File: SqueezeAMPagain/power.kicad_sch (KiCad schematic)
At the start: 63 parts, among them J6 Conn_01x02_Pin, J7 Barrel_Jack_Switch_MountingPin, Q1 Q_NPN_BEC, Q10 AO3401A, Q3 AO3401A, Q6 Q_NPN_BEC, Q7 AO3401A, Q8 AO3401A, Q9 AO3401A, U5 TPS5430DDA, U7 AMS1117-3.3

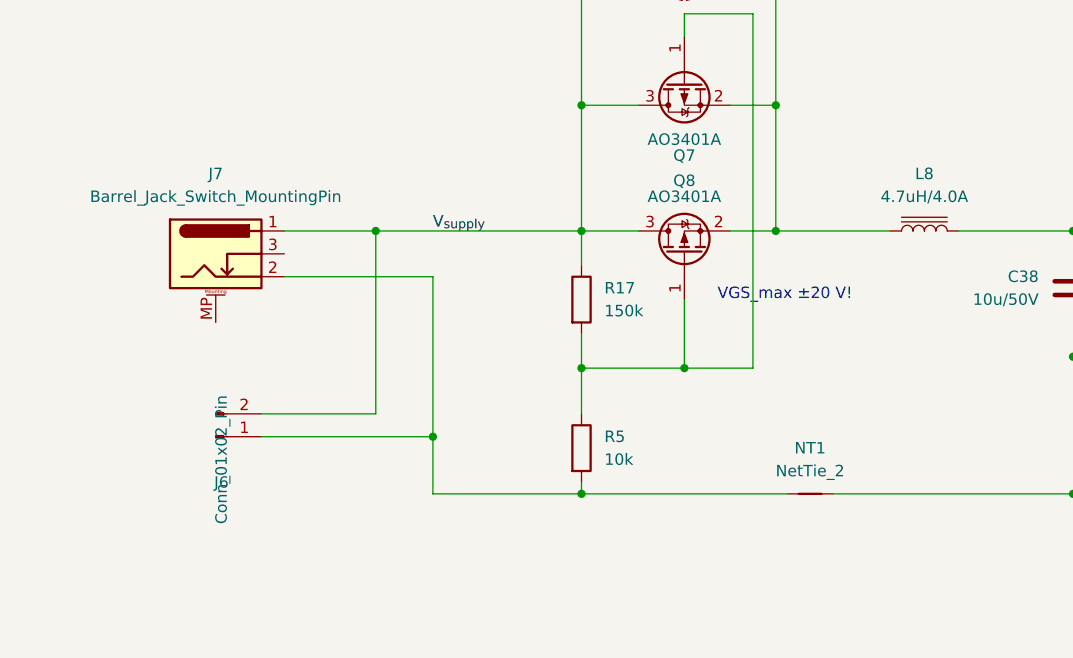
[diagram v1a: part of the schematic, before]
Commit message: Update SqueezeAMPagain.kicad_pcb, SqueezeAMPagain.kicad_prl, SqueezeAMPagain.kicad_pro, and 5 more files
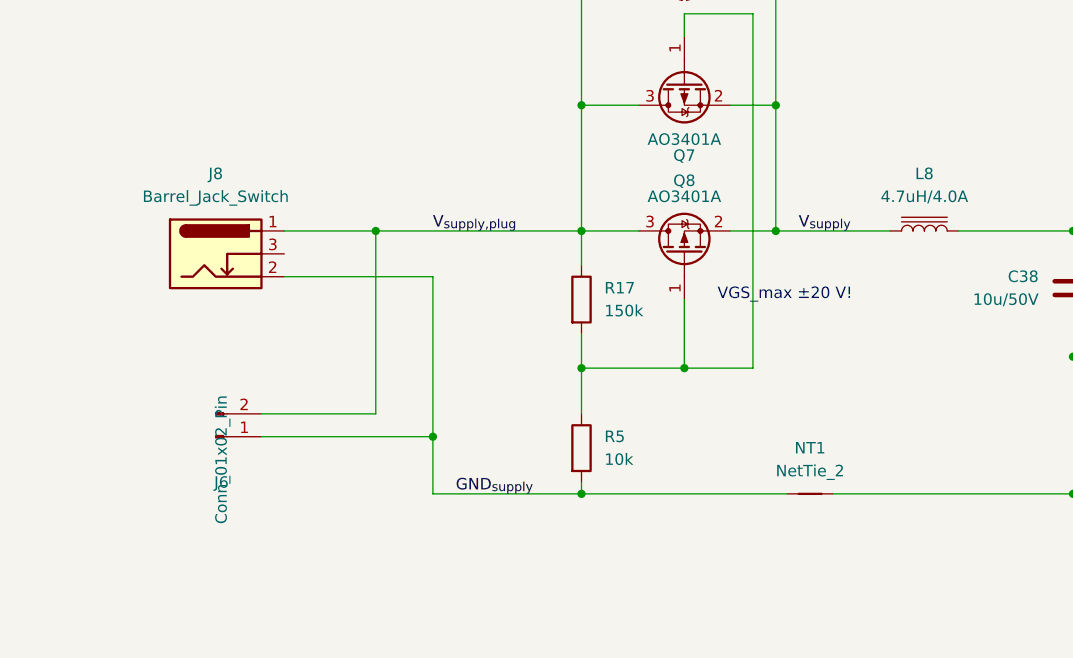
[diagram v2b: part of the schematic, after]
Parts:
- removed J7: Barrel_Jack_Switch_MountingPin, Connector_BarrelJack:BarrelJack_CUI_PJ-079BH_Horizontal, symbol Connector:Barrel_Jack_Switch_MountingPin
- added J8: Barrel_Jack_Switch, Connector_BarrelJack:BarrelJack_CUI_PJ-102AH_Horizontal, symbol Connector:Barrel_Jack_Switch
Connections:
- net V_{supply}: now also JP3.2 (B), L8.1, Q7.2 (S), Q8.2 (S); no longer J6.2 (Pin_2), JP3.1 (A), Q7.3 (D), Q8.3 (D), R17.1
- net GND_{supply}: now reaches J6.1 (Pin_1), NT1.1, R5.2
- net GND_{supply}: now also J8.2
- new net V_{supply,plug}: J6.2 (Pin_2), J8.1, JP3.1 (A), Q7.3 (D), Q8.3 (D), R17.1
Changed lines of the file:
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@@
 		)
 	)
+	(label "GND_{supply}"
+		(at 60.96 82.55 0)
+		(fields_autoplaced yes)
+		(effects
+			(font
+				(size 1.27 1.27)
+			)
+			(justify left bottom)
+		)
+	)
 	(label "PH"
 		(at 168.91 123.19 0)
@@
 	)
 	(label "V_{supply}"
+		(at 99.06 53.34 0)
+		(fields_autoplaced yes)
+		(effects
+			(font
+				(size 1.27 1.27)
+			)
+			(justify left bottom)
+		)
+	)
+	(label "V_{supply,plug}"
 		(at 58.42 53.34 0)
 		(fields_autoplaced yes)
@@
 		(length 2.54)
 		(shape round)
+		(at 82.55 177.8 0)
+		(fields_autoplaced yes)
+		(effects
+			(font
+				(size 1.27 1.27)
+			)
+			(justify left bottom)
+		)
+		(property "Netclass" "Supply"
+			(at 83.2485 175.26 0)
+			(effects
+				(font
+					(size 1.27 1.27)
+					(italic yes)
+				)
+				(justify left)
+			)
+		)
+	)
+	(netclass_flag ""
+		(length 2.54)
+		(shape round)
 		(at 153.67 53.34 0)
 		(fields_autoplaced yes)
@@
 	)
 	(symbol
-		(lib_id "Connector:Barrel_Jack_Switch_MountingPin")
-		(at 34.29 55.88 0)
-		(unit 1)
-		(exclude_from_sim no)
-		(in_bom yes)
-		(on_board yes)
-		(dnp no)
-		(fields_autoplaced yes)
-		(property "Reference" "J7"
-			(at 34.29 46.99 0)
-			(effects
-				(font
-					(size 1.27 1.27)
-				)
-			)
-		)
-		(property "Value" "Barrel_Jack_Switch_MountingPin"
-			(at 34.29 49.53 0)
-			(effects
-				(font
-					(size 1.27 1.27)
-				)
-			)
-		)
-		(property "Footprint" "Connector_BarrelJack:BarrelJack_CUI_PJ-079BH_Horizontal"
-			(at 35.56 56.896 0)
-			(effects
-				(font
-					(size 1.27 1.27)
-				)
-				(hide yes)
-			)
-		)
-		(property "Datasheet" "~"
-			(at 35.56 56.896 0)
-			(effects
-				(font
-					(size 1.27 1.27)
-				)
-				(hide yes)
-			)
-		)
-		(property "Description" "DC Barrel Jack with an internal switch and a mounting pin"
-			(at 34.29 55.88 0)
-			(effects
-				(font
-					(size 1.27 1.27)
-				)
-				(hide yes)
-			)
-		)
-		(pin "1"
-		)
-		(pin "MP"
-		)
-		(pin "3"
-		)
-		(pin "2"
-		)
-		(instances
-			(project ""
-				(path "/3675160b-d9e5-490e-b506-2a7966e79ed0/0f57a469-41de-4f06-810e-cfdb6f5b9e50"
-					(reference "J7")
-					(unit 1)
-				)
-			)
-		)
-	)
-	(symbol
 		(lib_id "power:GND")
 		(at 147.32 153.67 0)
@@
 					(unit 1)
 				)
+			)
+		)
+	)
+	(symbol
+		(lib_id "Connector:Barrel_Jack_Switch")
+		(at 34.29 55.88 0)
+		(unit 1)
+		(exclude_from_sim no)
+		(in_bom yes)
+		(on_board yes)
+		(dnp no)
+		(fields_autoplaced yes)
+		(property "Reference" "J8"
+			(at 34.29 46.99 0)
+			(effects
+				(font
+					(size 1.27 1.27)
+				)
+			)
+		)
+		(property "Value" "Barrel_Jack_Switch"
+			(at 34.29 49.53 0)
+			(effects
+				(font
+					(size 1.27 1.27)
+				)
+			)
+		)
+		(property "Footprint" "Connector_BarrelJack:BarrelJack_CUI_PJ-102AH_Horizontal"
+			(at 35.56 56.896 0)
+			(effects
+				(font
+					(size 1.27 1.27)
+				)
+				(hide yes)
+			)
+		)
+		(property "Datasheet" "~"
+			(at 35.56 56.896 0)
+			(effects
+				(font
+					(size 1.27 1.27)
+				)
+				(hide yes)
+			)
+		)
+		(property "Description" "DC Barrel Jack with an internal switch"
+			(at 34.29 55.88 0)
+			(effects
+				(font
+					(size 1.27 1.27)
+				)
+				(hide yes)
+			)
+		)
+		(property "reichelt#" "CLIFF FCR681465P"
+			(at 34.29 55.88 0)
+			(effects
+				(font
+					(size 1.27 1.27)
+				)
+				(hide yes)
+			)
+		)
+		(pin "1"
+		)
+		(pin "3"
+		)
+		(pin "2"
+		)
+		(instances
+			(project ""
+				(path "/3675160b-d9e5-490e-b506-2a7966e79ed0/0f57a469-41de-4f06-810e-cfdb6f5b9e50"
+					(reference "J8")
+					(unit 1)
+				)

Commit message: Update SqueezeAMPagain.kicad_pcb, SqueezeAMPagain.kicad_prl, SqueezeAMPagain.kicad_pro, and 11 more files
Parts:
- renumbered C76 to C59, C81 to C60, C2 to C62, C45 to C63, C71 to C64, C58 to C65, C38 to C66, C6 to C67, C42 to C68, C49 to C69, C51 to C70, C50 to C71, C59 to C72, C4 to C73, C44 to C74, C60 to C75, C43 to C76, C54 to C77, C82 to C78, C8 to C79, C57 to C80, C56 to C81, C83 to C82, D3 to D1, FB7 to FB2, FB2 to FB3, FB5 to FB4, FB1 to FB5, J8 to J6, J6 to J7, JP5 to JP10, JP3 to JP11, JP4 to JP12, JP12 to JP13, L8 to L5, L11 to L6, L9 to L7, Q6 to Q1, Q10 to Q2, Q7 to Q3, Q8 to Q4, Q1 to Q5, Q3 to Q6, Q9 to Q7, R19 to R22, R15 to R23, R18 to R24, R16 to R25, R17 to R26, R5 to R27, R20 to R28, R2 to R29, R4 to R30, R3 to R31, R14 to R32, R12 to R33, R13 to R34, U7 to U5, U5 to U6

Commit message: Update SqueezeAMPagain.kicad_pcb, SqueezeAMPagain.kicad_prl, SqueezeAMPagain.kicad_pro, and 4 more files
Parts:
- added C90: 2.2u/25V, Capacitor_SMD:C_0805_2012Metric, symbol Device:C
- added C91: 100n, Capacitor_SMD:C_0603_1608Metric, symbol Device:C
- added Q10: AO3401A, Package_TO_SOT_SMD:SOT-23, symbol Transistor_FET:AO3401A
- added Q11: Q_NPN_BEC, Package_TO_SOT_SMD:SOT-23, symbol Device:Q_NPN_BEC
- added R40: 150k, Resistor_SMD:R_0603_1608Metric, symbol Device:R
- added R41, R42: 10k, Resistor_SMD:R_0603_1608Metric, symbol Device:R
- D2: value SS34 550mV 2A -> SS34 550mV 2A
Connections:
- net +3.3V: now also Q10.2 (S), R40.1
- net GND: now also C90.2, C91.2, Q11.2 (E), R42.2
- net PON: now also R41.1
- new net: Q10.1 (G), Q11.3 (C), R40.2
- new net: Q11.1 (B), R41.2, R42.1
- new net +3.3V_{SW}: C90.1, C91.1, Q10.3 (D)
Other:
- moved on the sheet: C59, C60, C64, FB3, U5

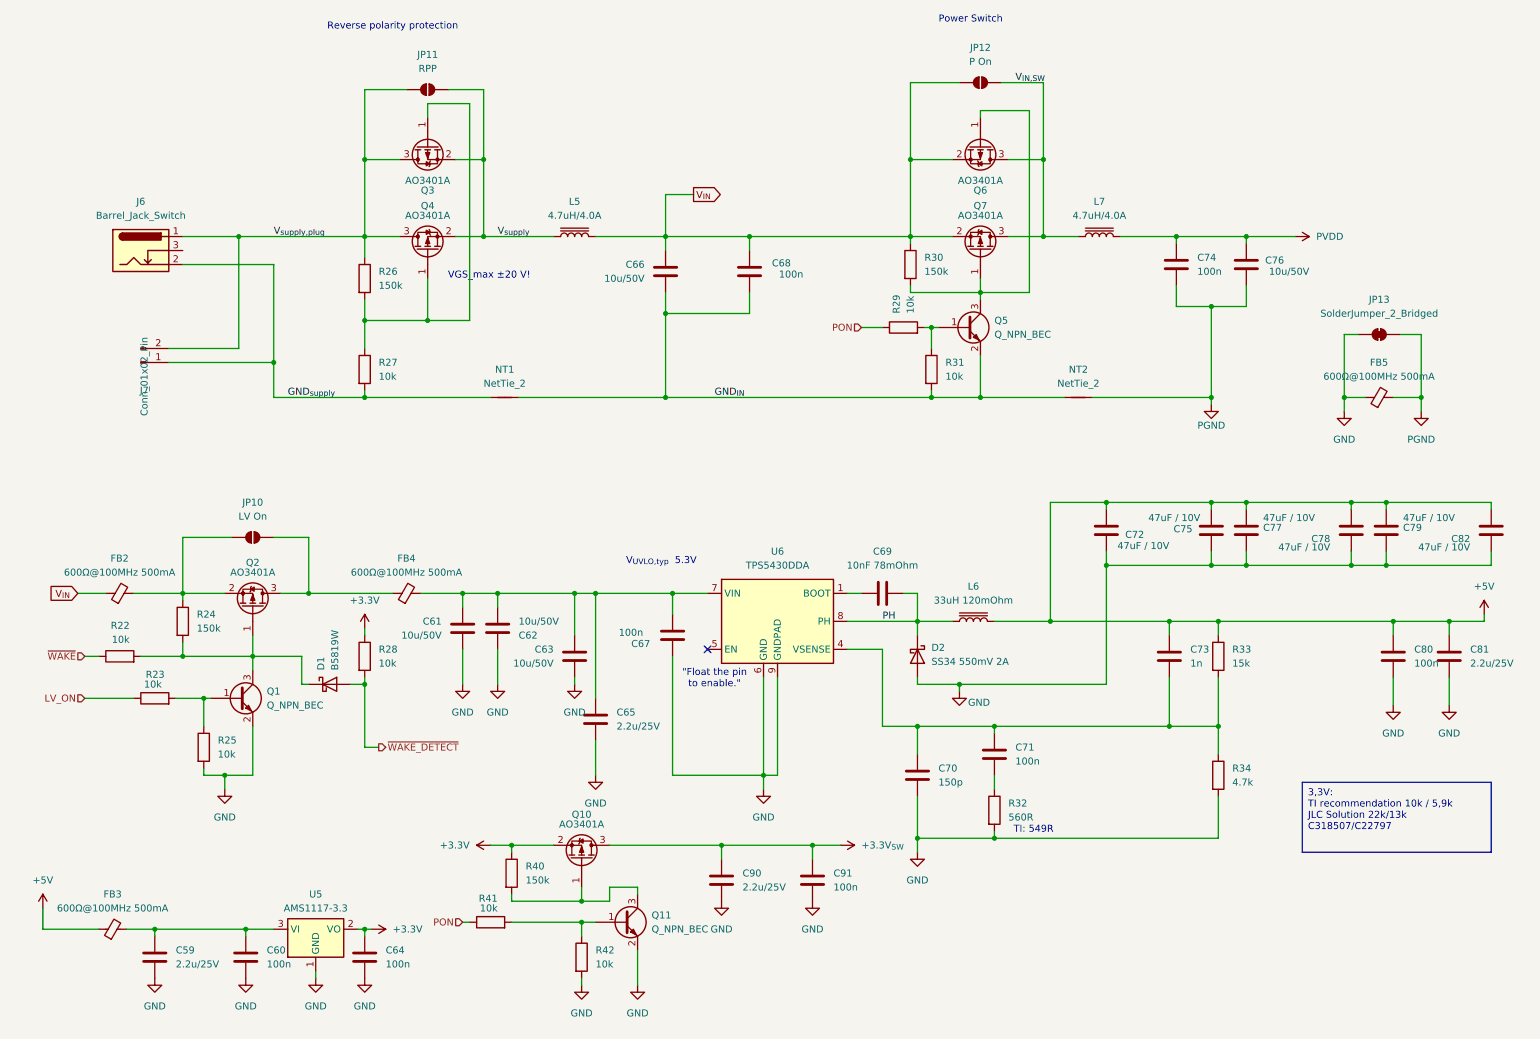
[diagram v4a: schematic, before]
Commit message: Update SqueezeAMPagain.kicad_pcb, SqueezeAMPagain.kicad_prl, SqueezeAMPagain.kicad_pro, and 5 more files
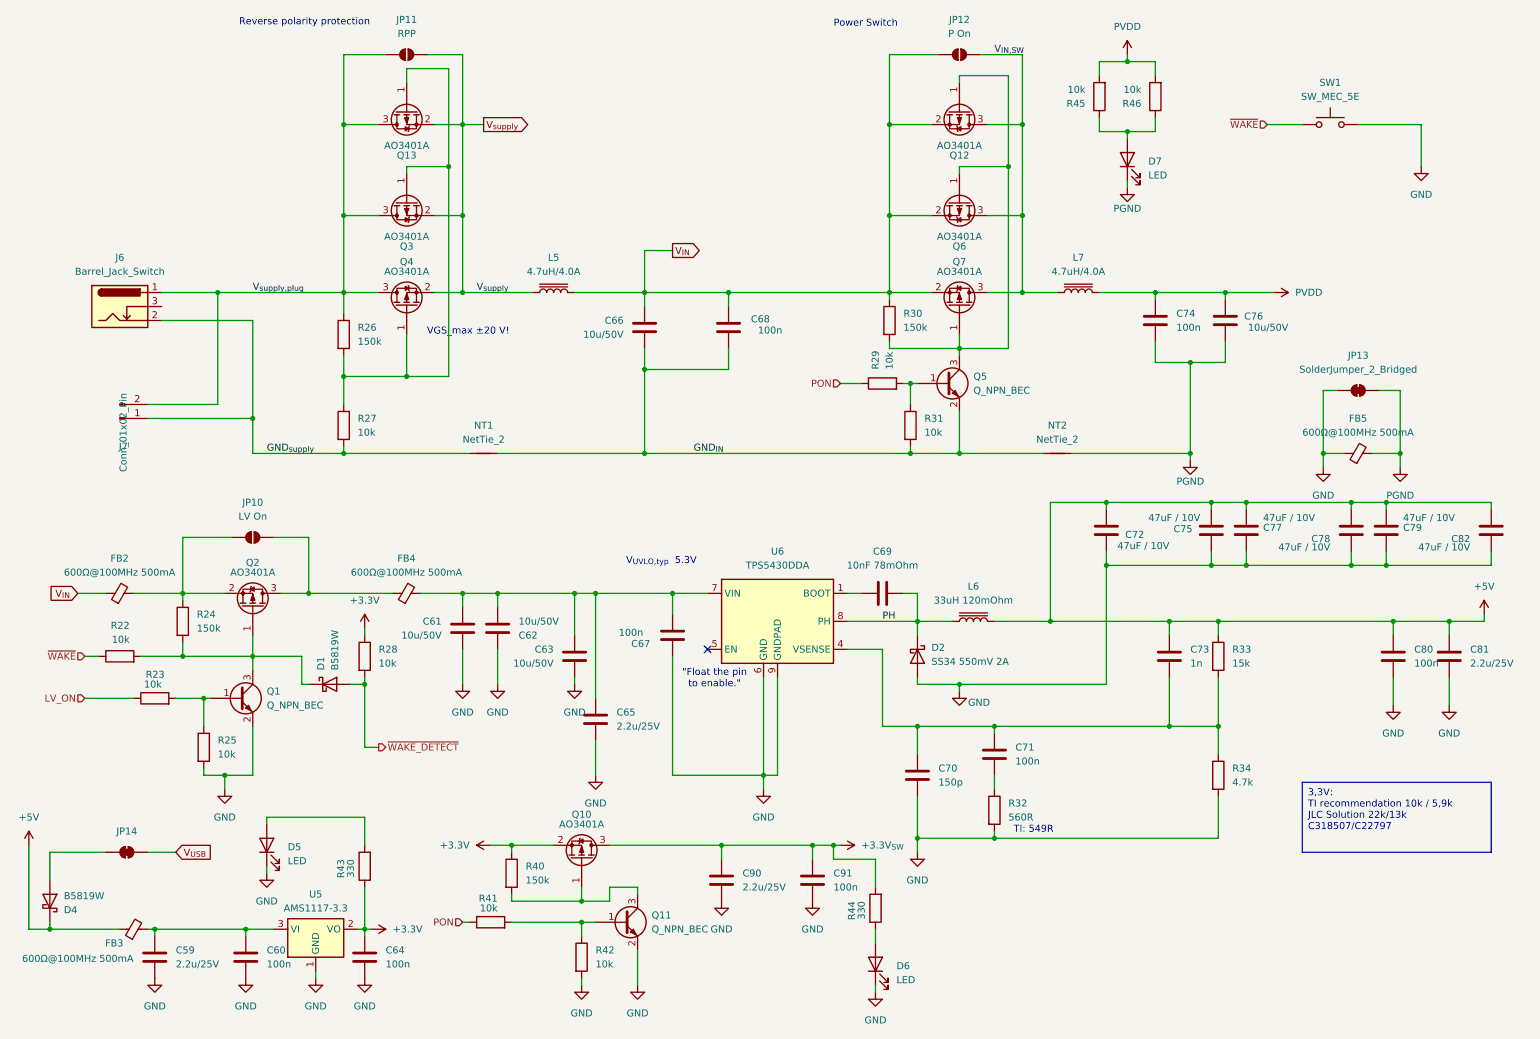
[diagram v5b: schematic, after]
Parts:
- added D4: B5819W, Diode_SMD:D_SOD-123, symbol Device:D_Schottky
- added D5, D6, D7: LED, LED_SMD:LED_0603_1608Metric, symbol Device:LED
- added JP14: SolderJumper_2_Bridged, Jumper:SolderJumper-2_P1.3mm_Bridged_RoundedPad1.0x1.5mm, symbol Jumper:SolderJumper_2_Bridged
- added Q12, Q13: AO3401A, Package_TO_SOT_SMD:SOT-23, symbol Transistor_FET:AO3401A
- added R43, R44: 330, Resistor_SMD:R_0603_1608Metric, symbol Device:R
- added R45, R46: 10k, Resistor_SMD:R_0603_1608Metric, symbol Device:R
- added SW1: SW_MEC_5E, Button_Switch_SMD:SW_Push_1P1T_XKB_TS-1187A, symbol Switch:SW_Push
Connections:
- net +3.3V: now also R43.1
- net +3.3V_{SW}: now also R44.2
- net +5V: now also D4.1 (K)
- net GND: now also D5.1 (K), D6.1 (K), SW1.2
- net PGND: now also D7.1 (K)
- net PVDD: now also R45.2, R46.2
- net V_{IN,SW}: now also Q12.3 (D)
- net V_{IN}: now also Q12.2 (S)
- net V_{supply,plug}: now also Q13.3 (D)
- net V_{supply}: now also Q13.2 (S)
- net ~{WAKE}: now also SW1.1
- net at Q3.1 (G), Q4.1 (G), R26.2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: now also Q13.1 (G)
- net at Q5.3 (C), Q6.1 (G), Q7.1 (G)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: now also Q12.1 (G)
- new net: D5.2 (A), R43.2
- new net: D7.2 (A), R45.1, R46.1
- new net: D6.2 (A), R44.1
- new net: D4.2 (A), JP14.2 (B)
- new net V_{USB}: JP14.1 (A)
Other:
- moved on the sheet: C66, C68, C74, C76, FB3, FB5, J6, J7, JP11, JP12, JP13, L5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

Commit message: Update SqueezeAMPagain.kicad_pcb, SqueezeAMPagain.kicad_prl, project.db, and 1 more file
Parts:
- L6: footprint Inductor:L_Vishay_IHLP-3232 -> Inductor_SMD:L_Chilisin_BMRB00060612; jlcpcb (none) -> C475526
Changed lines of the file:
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@@
 			)
 		)
-		(property "Footprint" "Inductor:L_Vishay_IHLP-3232"
+		(property "Footprint" "Inductor_SMD:L_Chilisin_BMRB00060612"
 			(at 185.42 123.19 0)
 			(effects
@@
 			(at 185.42 123.19 90)
 			(effects
+				(font
+					(size 1.27 1.27)
+				)
+				(hide yes)
+			)
+		)
+		(property "jlcpcb" "C475526"
+			(at 185.42 123.19 90)
+			(effects

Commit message: Update SqueezeAMPagain.kicad_pcb, project.db, and power.kicad_sch
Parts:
- added D8: 10V, symbol Device:D_Zener
- R43, R44: JLCPCB# (none) -> C23138
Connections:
- net V_{supply,plug}: now also D8.1 (K)
- net at Q13.1 (G), Q3.1 (G), Q4.1 (G)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: now also D8.2 (A)
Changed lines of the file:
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@@
 	)
 	(junction
+		(at 63.5 63.5)
+		(diameter 0)
+		(color 0 0 0 0)
+	)
+	(junction
 		(at 116.84 118.11)
 		(diameter 0)
@@
 	(wire
 		(pts
+			(xy 63.5 63.5) (xy 71.12 63.5)
+		)
+		(stroke
+			(width 0)
+			(type default)
+		)
+	)
+	(wire
+		(pts
 			(xy 194.31 33.02) (xy 194.31 49.53)
 		)
@@
 	(wire
 		(pts
+			(xy 63.5 78.74) (xy 63.5 74.93)
+		)
+		(stroke
+			(width 0)
+			(type default)
+		)
+	)
+	(wire
+		(pts
 			(xy 160.02 163.83) (xy 161.29 163.83)
 		)
@@
 	(wire
 		(pts
+			(xy 63.5 63.5) (xy 63.5 67.31)
+		)
+		(stroke
+			(width 0)
+			(type default)
+		)
+	)
+	(wire
+		(pts
 			(xy 173.99 91.44) (xy 173.99 92.71)
 		)
@@
 	(wire
 		(pts
+			(xy 71.12 78.74) (xy 63.5 78.74)
+		)
+		(stroke
+			(width 0)
+			(type default)
+		)
+	)
+	(wire
+		(pts
 			(xy 218.44 31.75) (xy 218.44 34.29)
 		)
@@
 	(wire
 		(pts
-			(xy 48.26 63.5) (xy 71.12 63.5)
+			(xy 48.26 63.5) (xy 63.5 63.5)
 		)
 		(stroke
@@
 	)
 	(symbol
+		(lib_id "Device:D_Zener")
+		(at 63.5 71.12 270)
+		(unit 1)
+		(exclude_from_sim no)
+		(in_bom yes)
+		(on_board yes)
+		(dnp no)
+		(fields_autoplaced yes)
+		(property "Reference" "D8"
+			(at 66.04 69.8499 90)
+			(effects
+				(font
+					(size 1.27 1.27)
+				)
+				(justify left)
+			)
+		)
+		(property "Value" "10V"
+			(at 66.04 72.3899 90)
+			(effects
+				(font
+					(size 1.27 1.27)
+				)
+				(justify left)
+			)
+		)
+		(property "Footprint" ""
+			(at 63.5 71.12 0)
+			(effects
+				(font
+					(size 1.27 1.27)
+				)
+				(hide yes)
+			)
+		)
+		(property "Datasheet" "~"
+			(at 63.5 71.12 0)
+			(effects
+				(font
+					(size 1.27 1.27)
+				)
+				(hide yes)
+			)
+		)
+		(property "Description" "Zener diode"
+			(at 63.5 71.12 0)
+			(effects
+				(font
+					(size 1.27 1.27)
+				)
+				(hide yes)
+			)
+		)
+		(pin "1"
+		)
+		(pin "2"
+		)
+		(instances
+			(project ""
+				(path "/3675160b-d9e5-490e-b506-2a7966e79ed0/0f57a469-41de-4f06-810e-cfdb6f5b9e50"
+					(reference "D8")
+					(unit 1)
+				)
+			)
+		)
+	)
+	(symbol
 		(lib_id "Device:R")
 		(at 208.28 27.94 180)
@@
 			)
 		)
+		(property "JLCPCB#" "C23138"
+			(at 167.64 175.26 90)
+			(effects
+				(font
+					(size 1.27 1.27)
+				)
+				(hide yes)
+			)
+		)
 		(pin "1"
 		)
@@
 			(effects
 				(font
+					(size 1.27 1.27)
+				)
+				(hide yes)
+			)
+		)
+		(property "JLCPCB#" "C23138"
+			(at 74.93 167.64 90)
+			(effects
+				(font

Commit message: Update SqueezeAMPagain.kicad_pcb, SqueezeAMPagain.kicad_prl, SqueezeAMPagain.kicad_pro, and 7 more files
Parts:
- removed D8: 10V, symbol Device:D_Zener
- added D10, D8, D9: min. 1.4V_{ff}, LED_SMD:LED_0603_1608Metric, symbol Device:LED
- added R47: 10k, Resistor_SMD:R_0603_1608Metric, symbol Device:R
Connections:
- net V_{IN}: now also D9.2 (A)
- net V_{supply,plug}: now also D8.2 (A)
- net at Q13.1 (G), Q3.1 (G), Q4.1 (G)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: now also D8.1 (K)
- net at D1.1 (K), Q1.3 (C), Q2.1 (G)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: now also D10.1 (K)
- net at FB2.2, JP10.1 (A), Q2.2 (S)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: now also D10.2 (A)
- net at Q12.1 (G), Q6.1 (G), Q7.1 (G)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: now also D9.1 (K), R47.1; no longer Q5.3 (C)
- new net: Q5.3 (C), R47.2
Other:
- moved on the sheet: C61, C62, C63, C65, C67, C69, C70, C71, D1, D2, FB4, J6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
